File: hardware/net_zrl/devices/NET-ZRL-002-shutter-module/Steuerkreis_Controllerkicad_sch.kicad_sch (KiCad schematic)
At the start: 14 parts

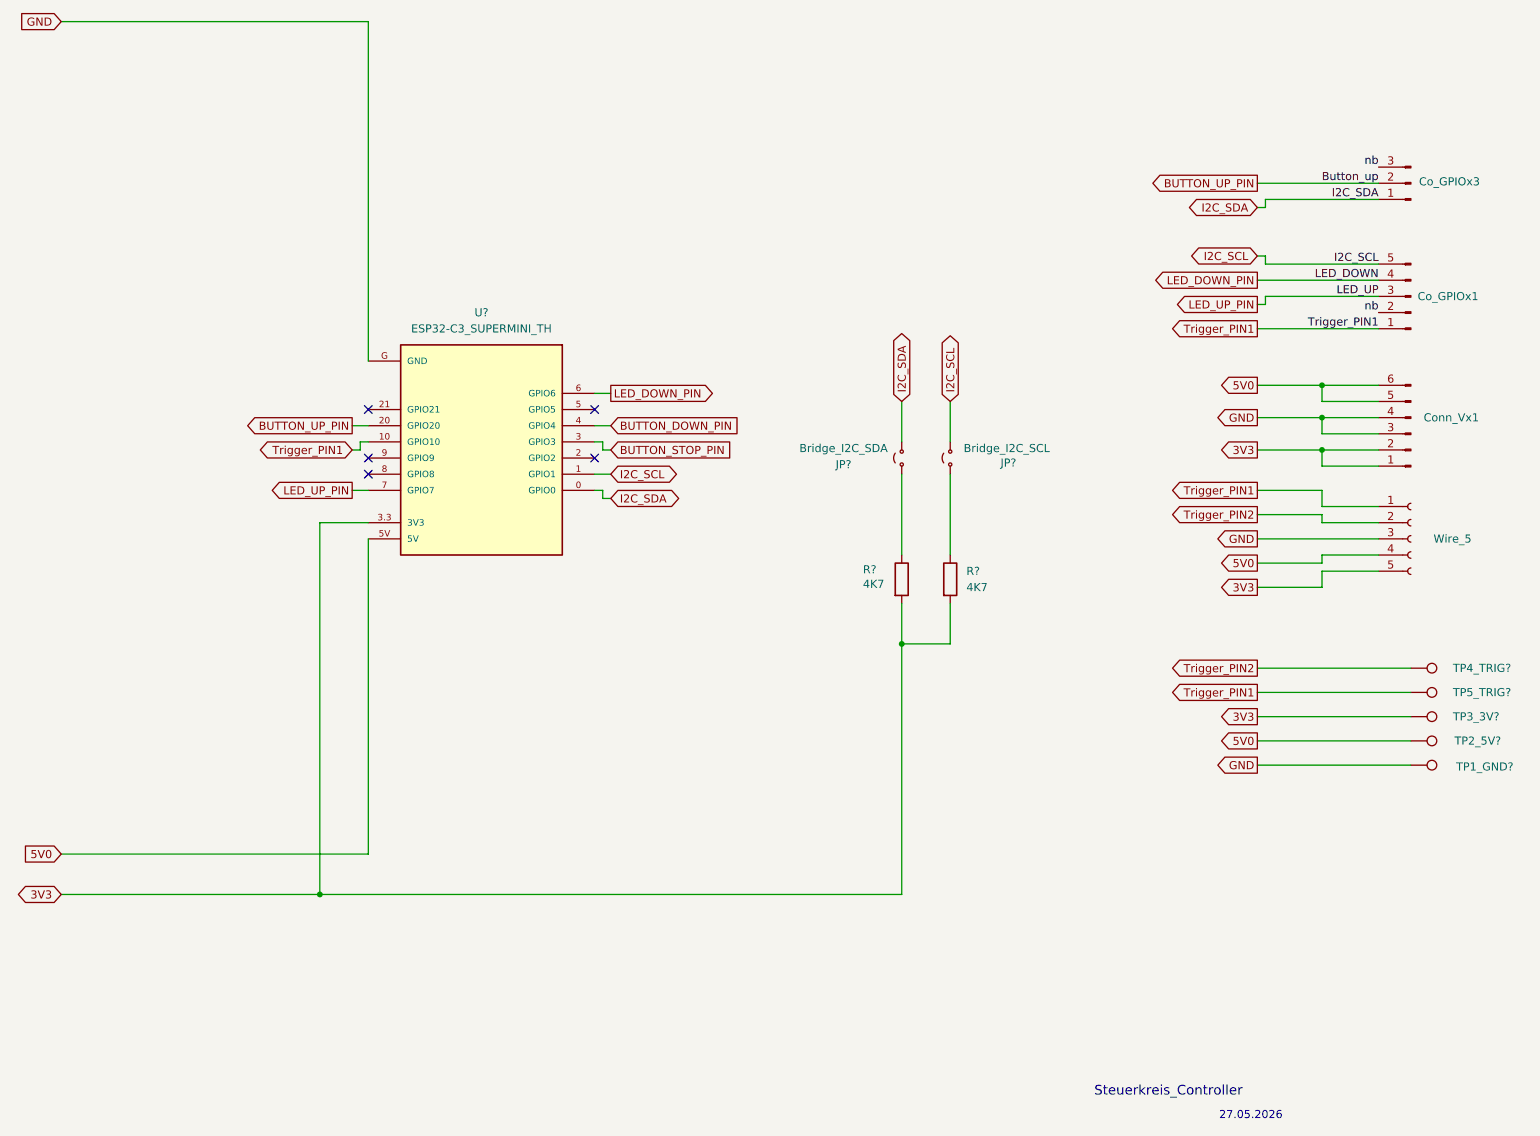
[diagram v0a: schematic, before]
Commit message: öffentliche Präsentation bereinigt: KI-Referenzen entfernt, READMEs optimiert, Firmware als Hauptlinie, ESPHome als Alternative mit Disclaimer
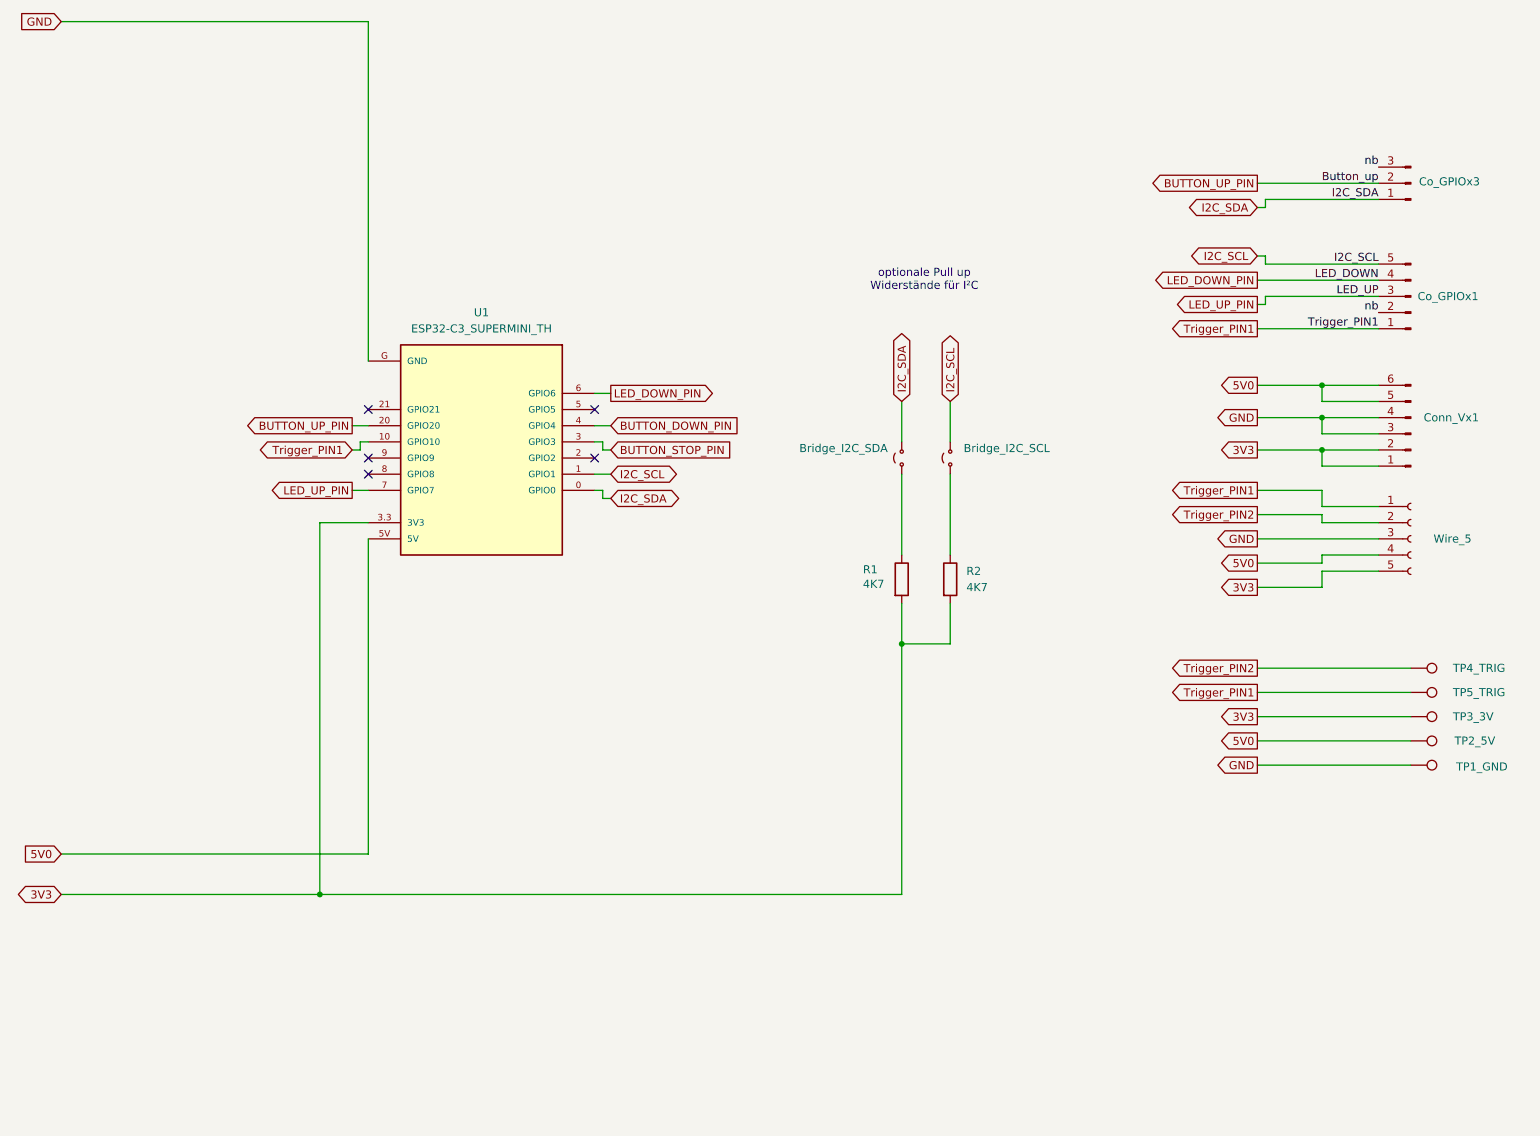
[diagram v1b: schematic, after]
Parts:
- gave numbers to parts that had none: 8
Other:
- note added: "optionale Pull up Widerstände für I²C"
- note removed: "27.05.2026"
- note removed: "Steuerkreis_Controller"
- title: (none) -> Steuerkreis_Controller
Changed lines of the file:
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@@
 	(generator_version "9.0")
 	(paper "A4")
-	(text "27.05.2026"
+	(title_block
+		(title "Steuerkreis_Controller")
+		(date "2026-05-29")
+		(comment 1 "Modularer Steuerkreis")
+	)
+	(text "optionale Pull up \nWiderstände für I²C"
 		(exclude_from_sim no)
-		(at 212.344 193.548 0)
-		(effects
-			(font
-				(size 1.27 1.27)
-			)
-		)
-	)
-	(text "Steuerkreis_Controller"
-		(exclude_from_sim no)
-		(at 199.39 189.738 0)
-		(effects
-			(font
-				(size 1.524 1.524)
+		(at 161.036 62.23 0)
+		(effects
+			(font
+				(size 1.27 1.27)
 			)
 		)
@@
 		(dnp no)
 		(fields_autoplaced yes)
-		(property "Reference" "R?"
+		(property "Reference" "R2"
 			(at 167.64 107.9499 0)
 			(effects
@@
 			(project "NET-ERL-001-hall-module"
 				(path "/08b3ce9e-6d39-416d-8082-65cb5f635528/d5b3e638-d147-42f1-9b4c-13afd73dd6cd"
-					(reference "R?")
+					(reference "R2")
 					(unit 1)
 				)
@@
 		(on_board yes)
 		(dnp no)
-		(property "Reference" "TP5_TRIG?"
+		(property "Reference" "TP5_TRIG"
 			(at 244.094 127 90)
 			(effects
@@
 			(project "NET-ERL-001-hall-module"
 				(path "/08b3ce9e-6d39-416d-8082-65cb5f635528/d5b3e638-d147-42f1-9b4c-13afd73dd6cd"
-					(reference "TP5_TRIG?")
+					(reference "TP5_TRIG")
 					(unit 1)
 				)
@@
 		(on_board yes)
 		(dnp no)
-		(property "Reference" "TP1_GND?"
+		(property "Reference" "TP1_GND"
 			(at 244.602 138.684 90)
 			(effects
@@
 			(project "NET-ERL-001-hall-module"
 				(path "/08b3ce9e-6d39-416d-8082-65cb5f635528/d5b3e638-d147-42f1-9b4c-13afd73dd6cd"
-					(reference "TP1_GND?")
+					(reference "TP1_GND")
 					(unit 1)
 				)
@@
 		(on_board yes)
 		(dnp no)
-		(property "Reference" "TP2_5V?"
+		(property "Reference" "TP2_5V"
 			(at 244.348 134.62 90)
 			(effects
@@
 			(project "NET-ERL-001-hall-module"
 				(path "/08b3ce9e-6d39-416d-8082-65cb5f635528/d5b3e638-d147-42f1-9b4c-13afd73dd6cd"
-					(reference "TP2_5V?")
+					(reference "TP2_5V")
 					(unit 1)
 				)
@@
 					(size 1.27 1.27)
 				)
+				(hide yes)
 			)
 		)
@@
 					(size 1.27 1.27)
 				)
+				(hide yes)
 			)
 		)
@@
 		(on_board yes)
 		(dnp no)
-		(property "Reference" "TP4_TRIG?"
+		(property "Reference" "TP4_TRIG"
 			(at 244.094 123.19 90)
 			(effects
@@
 			(project "NET-ERL-001-hall-module"
 				(path "/08b3ce9e-6d39-416d-8082-65cb5f635528/d5b3e638-d147-42f1-9b4c-13afd73dd6cd"
-					(reference "TP4_TRIG?")
+					(reference "TP4_TRIG")
 					(unit 1)
 				)
@@
 		(on_board yes)
 		(dnp no)
-		(property "Reference" "TP3_3V?"
+		(property "Reference" "TP3_3V"
 			(at 244.094 130.81 90)
 			(effects
@@
 			(project "NET-ERL-001-hall-module"
 				(path "/08b3ce9e-6d39-416d-8082-65cb5f635528/d5b3e638-d147-42f1-9b4c-13afd73dd6cd"
-					(reference "TP3_3V?")
+					(reference "TP3_3V")
 					(unit 1)
 				)
@@
 		(on_board yes)
 		(dnp no)
-		(property "Reference" "R?"
+		(property "Reference" "R1"
 			(at 151.384 107.696 0)
 			(effects
@@
 			(project "NET-ERL-001-hall-module"
 				(path "/08b3ce9e-6d39-416d-8082-65cb5f635528/d5b3e638-d147-42f1-9b4c-13afd73dd6cd"
-					(reference "R?")
+					(reference "R1")
 					(unit 1)
 				)
@@
 		(dnp no)
 		(fields_autoplaced yes)
-		(property "Reference" "U?"
+		(property "Reference" "U1"
 			(at 91.44 67.31 0)
 			(effects
@@
 			(project "NET-ERL-001-hall-module"
 				(path "/08b3ce9e-6d39-416d-8082-65cb5f635528/d5b3e638-d147-42f1-9b4c-13afd73dd6cd"
-					(reference "U?")
+					(reference "U1")
 					(unit 1)
 				)
